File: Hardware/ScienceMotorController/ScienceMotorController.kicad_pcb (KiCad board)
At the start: 2 copper layers, 124.5 x 108.5 mm, 120 parts, among them U1 LT1910, U10 PMN280ENEAX, U11 TB67H400AFNG,EL, U12 TB67H400AFNG,EL, U13 LT1910, U14 PMN280ENEAX, U15 LTC6900, U16 TB67H400AFNG,EL, U17 TB67H400AFNG,EL, U2 OKI, U3 OKI, U4 OKI, U5 TB67H400AFNG,EL, U6 TB67H400AFNG,EL, U7 PMN280ENEAX, U8 LT1910, U9 TM4C129E_Launchpad

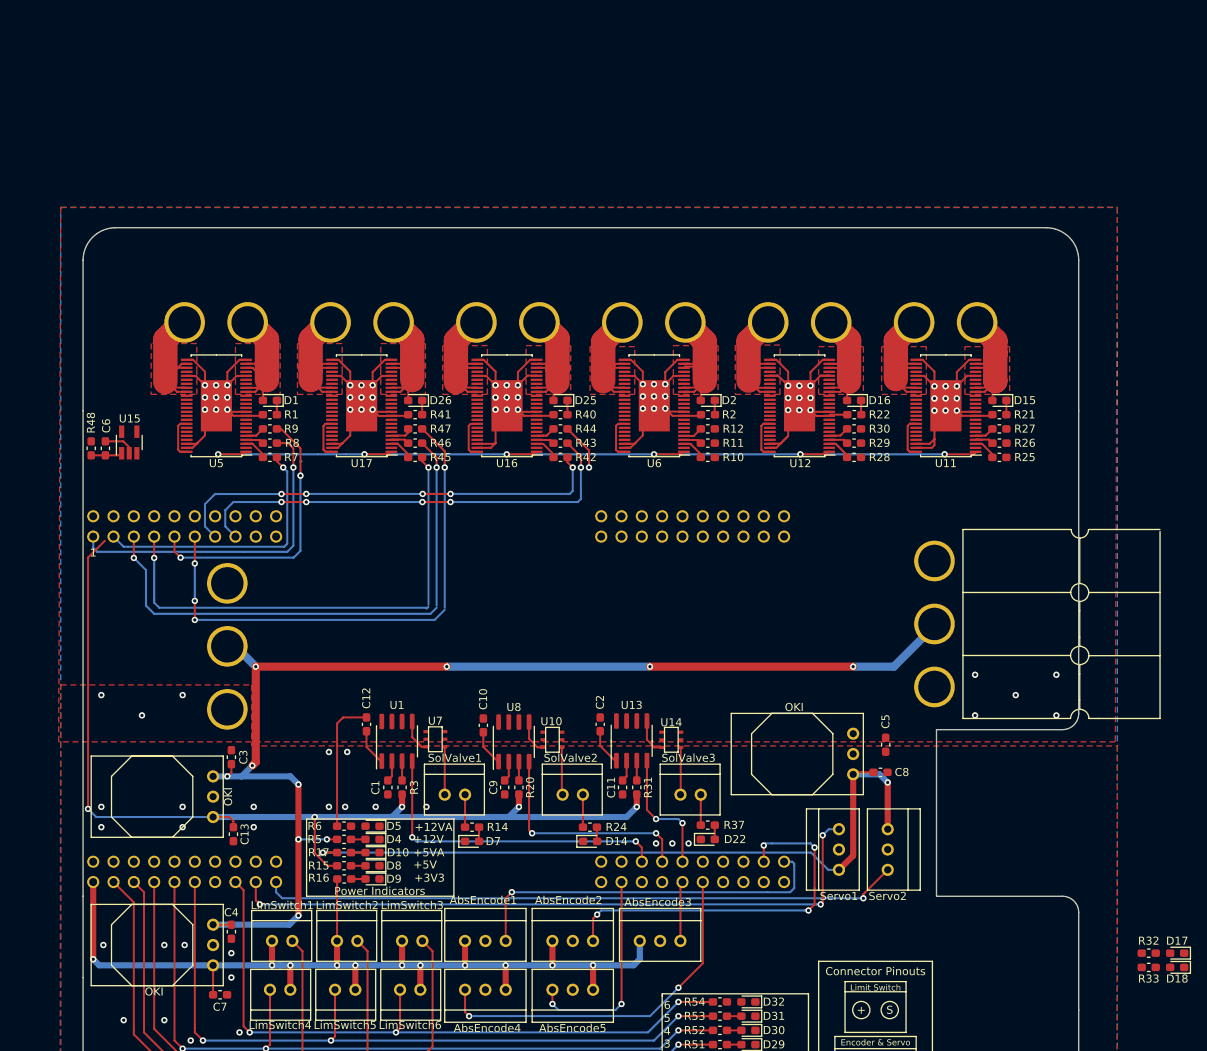
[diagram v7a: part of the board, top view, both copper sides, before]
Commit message: Completed Board and reviewed with Electrical Leadership
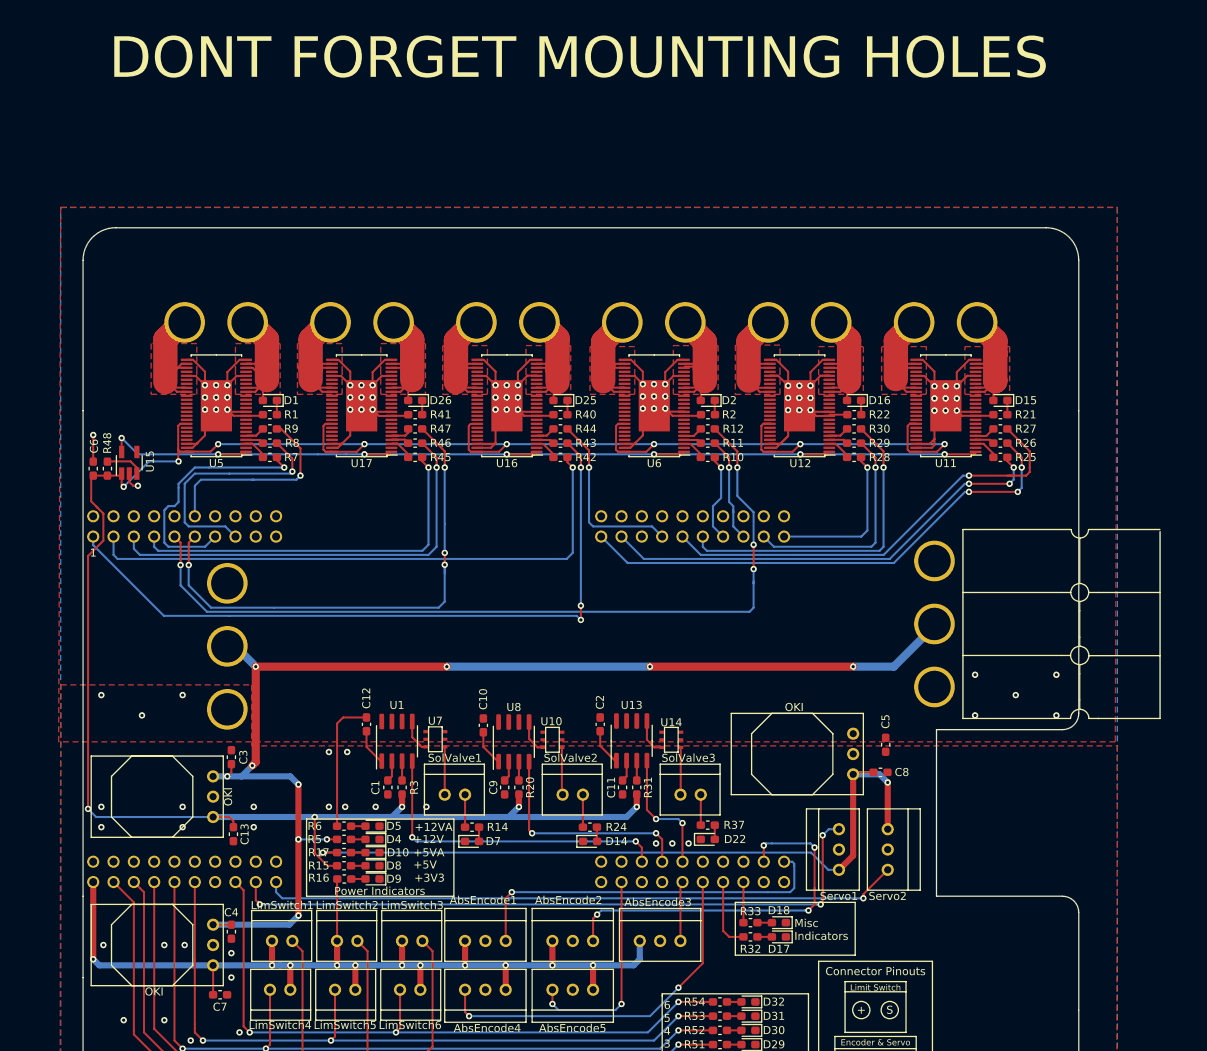
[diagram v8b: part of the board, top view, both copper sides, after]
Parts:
- moved R33 50.1 mm to (114.2, 163.1)
- moved D18 50.1 mm to (117.7, 163.1)
- moved R32 49.8 mm to (114.2, 164.8), turned to 0 degrees
- moved D17 49.8 mm to (117.7, 164.8)
- moved R48 3.25 mm to (33.8, 106.3)
- moved C6 2.96 mm to (32.0, 106.3)
- moved U15 2.54 mm to (36.5, 105.6)
- moved D15 0.13 mm to (145.4, 97.8)
- moved R21 0.13 mm to (145.4, 99.6)
- moved R25 0.13 mm to (145.4, 104.9)
- moved R27 0.13 mm to (145.4, 101.3)
- moved R26 0.11 mm to (145.4, 103.1)
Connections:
- R32 pad 1: Net-(D17-Pad2) -> Net-(R32-Pad1)
- R32 pad 2: Net-(R32-Pad2) -> Net-(D17-Pad2)
- U9 pad PD1: PWMA_4 -> PWMA_1
- U9 pad PF1: InA2_1 -> InA2_3
- U9 pad PF2: InA1_1 -> InA1_3
- U9 pad PG1: InA1_2 -> InA2_2
- U9 pad PH0: InA2_4 -> InA1_4
- U9 pad PH1: InA1_4 -> InA2_4
- U9 pad PK4: InA2_2 -> InA1_2
- U9 pad PL0: InA1_3 -> InA1_1
- U9 pad PL1: InA2_3 -> InA2_1
- U9 pad PL4: PWMA_1 -> PWMA_4
- U9 pad PM0: PWMA_2 -> PWMA_3
- U9 pad PM1: PWMA_3 -> PWMA_2
- U9 pad PP3: Net-(R33-Pad2) -> Net-(U9-PadPP3)
- U9 pad PP4: Net-(U9-PadPP4) -> Net-(R33-Pad2)
- U9 pad PQ0: Net-(U9-PadPQ0) -> Net-(R32-Pad1)
- U9 pad PQ2: Net-(R32-Pad2) -> Net-(U9-PadPQ2)
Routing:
- net +5V: track 160.4 -> 296.7 mm, vias 5 -> 13
- net PWMA_4: track 0.00 -> 104.2 mm, vias 0 -> 4
- net InA2_2: track 0.00 -> 64.2 mm, vias 0 -> 3
- net InA1_2: track 0.00 -> 57.4 mm, vias 0 -> 3
- net PWMA_2: track 0.00 -> 55.9 mm, vias 0 -> 1
- net PWMA_5: track 0.00 -> 40.2 mm, vias 0 -> 1
- net InA2_3: track 56.5 -> 88.7 mm, vias 5 -> 3
- net InA2_5: track 0.00 -> 27.9 mm, vias 0 -> 1
- net InA1_5: track 0.00 -> 20.2 mm, vias 0 -> 1
- net PWMA_3: track 5.94 -> 22.7 mm
- net InA1_3: track 55.7 -> 72.4 mm, vias 5 -> 1
- net Oscillator: track 113.6 -> 128.3 mm, vias 6 -> 7
- net InA1_6: track 61.8 -> 47.3 mm, vias 2 -> 1
- net InA2_6: track 67.6 -> 53.8 mm, vias 2 -> 1
- net InA2_4: track 0.00 -> 13.4 mm, vias 0 -> 1
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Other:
- board text added: "DONT FORGET MOUNTING HOLES"
- board text added: "Misc Indicators"
